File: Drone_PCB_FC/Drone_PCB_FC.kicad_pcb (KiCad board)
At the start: 2 copper layers, 59 parts, among them CN1 SM10B-SRSS-TB, J1 Conn_01x05, J2 USB_C_Receptacle_USB2.0_14P, J3 Conn_01x04, SW1 SW_Push, SW2 SW_Push, U1 AP2112K-3.3, U2 USBLC6-2SC6, U4 STM32F405RGTx, U5 TPS5430DDAR, U6 ICM-42605, U7 W25Q128JVE, Y1 8MHz

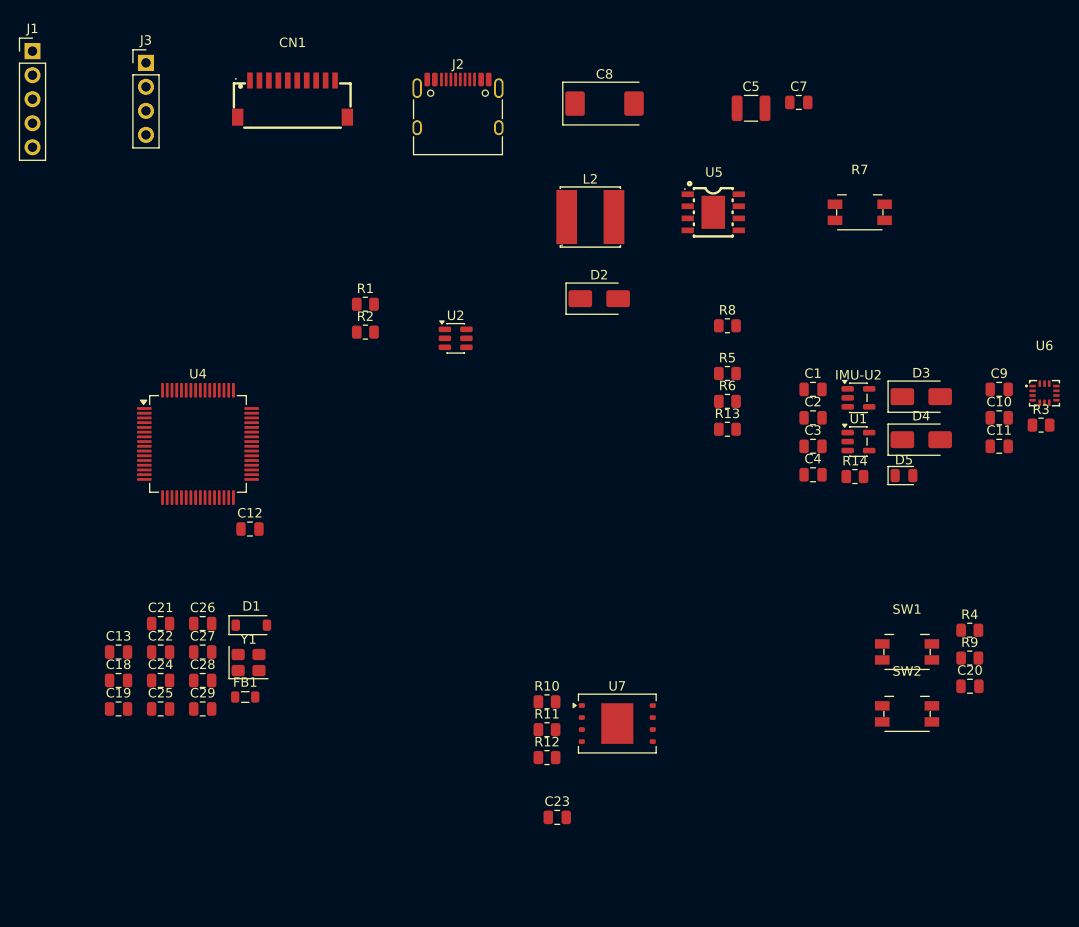
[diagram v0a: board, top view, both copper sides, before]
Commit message: pcb is 'done' but i think i messed up the IMU so ill fix later
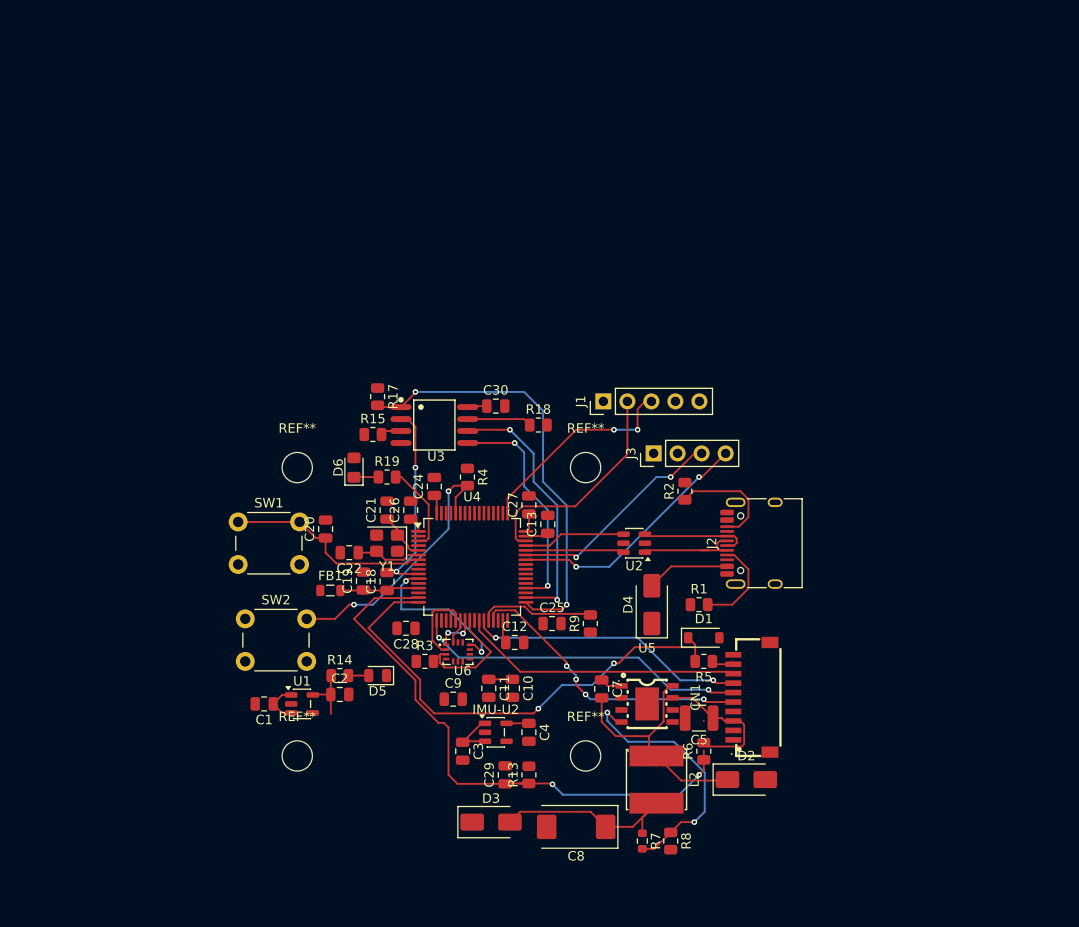
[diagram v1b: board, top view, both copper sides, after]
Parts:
- removed C23: 100nF, Capacitor_SMD:C_0805_2012Metric
- removed R10, R11, R12: 10k, Resistor_SMD:R_0805_2012Metric
- removed U7: W25Q128JVE, Package_SON:WSON-8-1EP_8x6mm_P1.27mm_EP3.4x4.3mm
- added C30: 100nF, Capacitor_SMD:C_0805_2012Metric, F.Cu at (124.5, 78.5)
- added D6: LED, LED_SMD:LED_0805_2012Metric_Pad1.15x1.40mm_HandSolder, F.Cu at (109.5, 85.0)
- added R15: 10k, Resistor_SMD:R_0805_2012Metric, F.Cu at (111.5, 81.5)
- added R17: 10k, Resistor_SMD:R_0805_2012Metric, F.Cu at (112.0, 77.5)
- added R18: 10k, Resistor_SMD:R_0805_2012Metric, F.Cu at (129.0, 80.5)
- added R19: 330, Resistor_SMD:R_0805_2012Metric, F.Cu at (113.0, 86.0)
- added REF**: MountingHole_3.2mm_M3, MountingHole:MountingHole_3.2mm_M3, F.Cu at (134.0, 85.0)
- added REF**: MountingHole_3.2mm_M3, MountingHole:MountingHole_3.2mm_M3, F.Cu at (103.5, 115.5)
- added REF**: MountingHole_3.2mm_M3, MountingHole:MountingHole_3.2mm_M3, F.Cu at (103.5, 85.0)
- added REF**: MountingHole_3.2mm_M3, MountingHole:MountingHole_3.2mm_M3, F.Cu at (134.0, 115.5)
- added U3: W25Q128JVSIQTR, drone_lib:SOIC-8_L5.3-W5.3-P1.27-LS8.0-BL, F.Cu at (118.0, 80.5)
- R7: footprint Button_Switch_SMD:Panasonic_EVQPUJ_EVQPUA -> Resistor_SMD:R_0603_1608Metric
- SW1, SW2: footprint Button_Switch_SMD:Panasonic_EVQPUJ_EVQPUA -> Button_Switch_THT:SW_PUSH_6mm
- moved CN1 79.8 mm to (151.6, 109.3), turned to 90 degrees
- moved C8 76.6 mm to (133.0, 123.0), turned to 180 degrees
- moved SW1 72.1 mm to (97.2, 90.8)
- moved J1 70.8 mm to (135.9, 78.0), turned to 90 degrees
- moved SW2 70.7 mm to (98.0, 101.0)
- moved R7 70.4 mm to (140.0, 124.5), turned to -90 degrees
- moved C20 70.1 mm to (106.5, 91.5), turned to 90 degrees
- moved R3 69.8 mm to (117.0, 105.5)
- moved U6 67.8 mm to (120.5, 104.5)
- moved J3 67.7 mm to (141.2, 83.5), turned to 90 degrees
- moved C1 66.9 mm to (100.0, 110.0), turned to 180 degrees
- moved C9 66.4 mm to (120.0, 109.5)
- moved C7 65.4 mm to (135.7, 108.4), turned to -90 degrees
- moved U1 65.1 mm to (104.0, 110.0)
- moved C5 64.7 mm to (146.0, 111.5), turned to 180 degrees
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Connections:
- C29 pad 1: Net-(U4-PC2) -> Net-(U4-PA1)
- CN1 pad 5: TIM3_CH2-M4 -> TIM2_CH3-M4
- CN1 pad 6: TIM4_CH1-M3 -> TIM2_CH4-M3
- R13 pad 1: Net-(U4-PC2) -> Net-(U4-PA1)
- R6 pad 1: Net-(U4-PC2) -> Net-(U4-PA1)
- U4 pad 10: Net-(U4-PC2) -> SPI2_MISO
- U4 pad 15: unconnected-(U4-PA1-Pad15) -> Net-(U4-PA1)
- U4 pad 16: unconnected-(U4-PA2-Pad16) -> Net-(D1-K)
- U4 pad 17: unconnected-(U4-PA3-Pad17) -> TIM2_CH4-M3
- U4 pad 25: unconnected-(U4-PC5-Pad25) -> Net-(BZ1-+)
- U4 pad 29: unconnected-(U4-PB10-Pad29) -> TIM2_CH3-M4
- U4 pad 3: unconnected-(U4-PC14-Pad3) -> Net-(U4-PC14)
- U4 pad 35: SPI2_MISO -> unconnected-(U4-PB14-Pad35)
- U4 pad 57: TIM3_CH2-M4 -> unconnected-(U4-PB5-Pad57)
- U4 pad 58: TIM4_CH1-M3 -> unconnected-(U4-PB6-Pad58)
- U4 pad 9: Net-(D1-K) -> unconnected-(U4-PC1-Pad9)
- U6 pad 1: MISO -> MOSI
- U6 pad 10: GND -> +3V3
- U6 pad 11: GND -> EXTI3
- U6 pad 12: nCS -> GND
- U6 pad 13: SPI1_SCK -> GND
- U6 pad 14: MOSI -> MISO
- U6 pad 2: GND -> SPI1_SCK
- U6 pad 3: GND -> nCS
- U6 pad 4: EXTI3 -> GND
- U6 pad 5: +3V3 -> GND
- U6 pad 7: GND -> +3V3_IMU
- U6 pad 8: +3V3_IMU -> GND
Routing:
- net Net-(U4-PA1): track 0.00 -> 60.8 mm, vias 0 -> 2
- net Net-(D1-K): track 0.00 -> 51.6 mm, vias 0 -> 2
- net /CS: track 0.00 -> 45.5 mm, vias 0 -> 2
- net TIM2_CH4-M3: track 0.00 -> 35.5 mm, vias 0 -> 2
- net TIM2_CH3-M4: track 0.00 -> 31.2 mm, vias 0 -> 4
- net TIM3_CH4-M2: track 0.00 -> 30.3 mm, vias 0 -> 2
- net TIM3_CH3-M1: track 0.00 -> 29.8 mm
- net BOOT0: track 0.00 -> 28.6 mm, vias 0 -> 2
- net SPI2_SCK: track 0.00 -> 28.0 mm, vias 0 -> 2
- net Net-(U5-VSENSE): track 0.00 -> 27.7 mm, vias 0 -> 2
- net UARTx_TX: track 0.00 -> 26.4 mm, vias 0 -> 2
- net Net-(D2-K): track 0.00 -> 25.7 mm
- net SPI2_MOSI: track 0.00 -> 23.9 mm, vias 0 -> 2
- net SWDIO: track 0.00 -> 23.9 mm
- net UARTx_RX: track 0.00 -> 23.3 mm, vias 0 -> 2
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- added copper zone on In1.Cu, net GND
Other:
- copper layers 2 -> 4

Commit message: 3rd try on the PCB, still need to triple check before I order, and I NEED to check stock because i might need a redesign
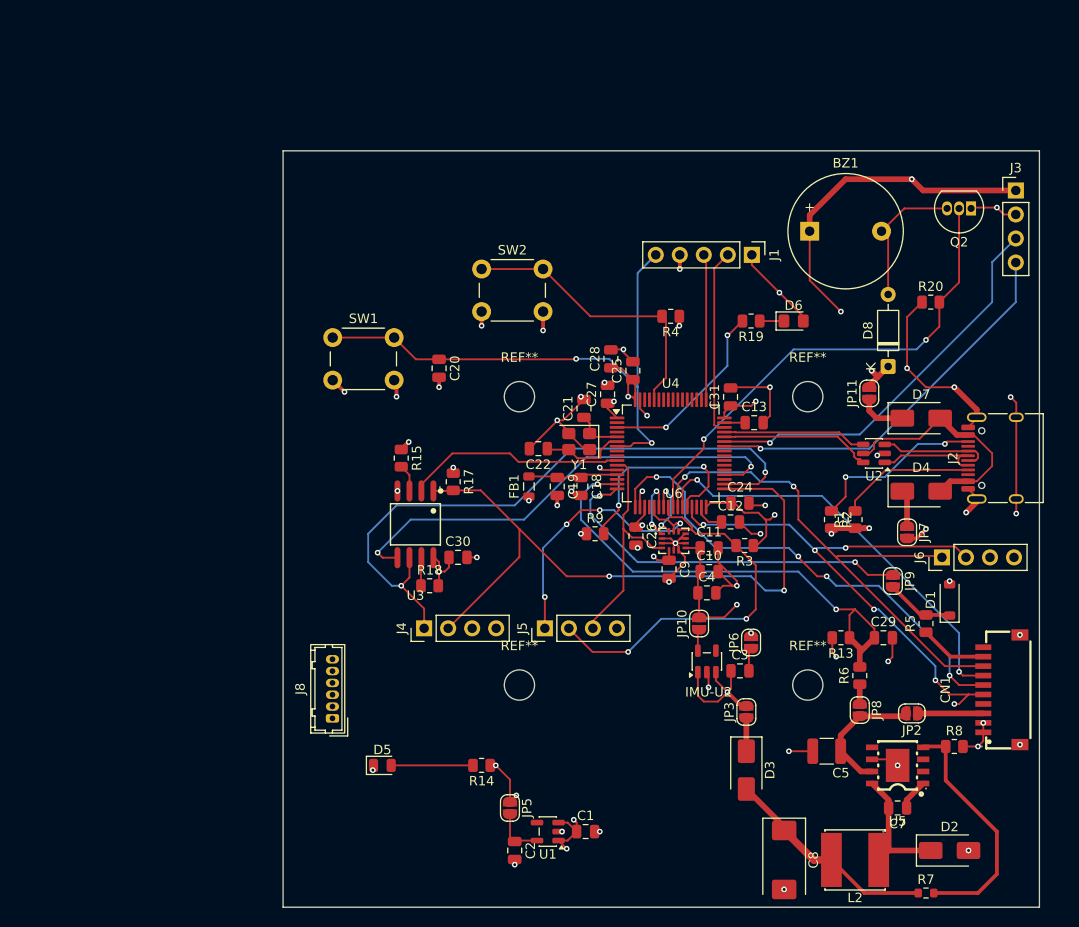
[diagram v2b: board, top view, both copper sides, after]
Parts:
- removed the REF** at (134.0, 85.0)
- removed the REF** at (103.5, 115.5)
- removed the REF** at (103.5, 85.0)
- removed the REF** at (134.0, 115.5)
- added BZ1: Buzzer, Buzzer_Beeper:Buzzer_12x9.5RM7.6, F.Cu at (157.7, 60.0)
- added C31: 100nF, Capacitor_SMD:C_0805_2012Metric, F.Cu at (149.3, 77.5)
- added D7: D_Schottky, Diode_SMD:D_SMA, F.Cu at (169.5, 79.8)
- added D8: 1N914, Diode_THT:D_DO-35_SOD27_P7.62mm_Horizontal, F.Cu at (166.0, 74.3)
- added J4: Conn_01x04, Connector_PinHeader_2.54mm:PinHeader_1x04_P2.54mm_Vertical, F.Cu at (116.9, 102.0)
- added J5: Conn_01x04, Connector_PinHeader_2.54mm:PinHeader_1x04_P2.54mm_Vertical, F.Cu at (129.7, 102.0)
- added J6: Conn_01x04, Connector_PinHeader_2.54mm:PinHeader_1x04_P2.54mm_Vertical, F.Cu at (171.7, 94.5)
- added J8: Conn_01x06, Connector_Hirose:Hirose_DF13-06P-1.25DSA_1x06_P1.25mm_Vertical, F.Cu at (107.2, 111.5)
- added JP10: SolderJumper_2_Open, Jumper:SolderJumper-2_P1.3mm_Open_RoundedPad1.0x1.5mm, F.Cu at (146.0, 101.5)
- added JP11: SolderJumper_2_Open, Jumper:SolderJumper-2_P1.3mm_Open_RoundedPad1.0x1.5mm, F.Cu at (164.0, 77.2)
- added JP2: SolderJumper_2_Open, Jumper:SolderJumper-2_P1.3mm_Open_RoundedPad1.0x1.5mm, F.Cu at (168.5, 111.0)
- added JP3: SolderJumper_2_Open, Jumper:SolderJumper-2_P1.3mm_Open_RoundedPad1.0x1.5mm, F.Cu at (151.0, 110.8)
- added JP5: SolderJumper_2_Open, Jumper:SolderJumper-2_P1.3mm_Open_RoundedPad1.0x1.5mm, F.Cu at (126.0, 121.0)
- added JP6: SolderJumper_2_Open, Jumper:SolderJumper-2_P1.3mm_Open_RoundedPad1.0x1.5mm, F.Cu at (151.5, 103.5)
- added JP7: SolderJumper_2_Open, Jumper:SolderJumper-2_P1.3mm_Open_RoundedPad1.0x1.5mm, F.Cu at (168.0, 91.8)
- added JP8: SolderJumper_2_Open, Jumper:SolderJumper-2_P1.3mm_Open_RoundedPad1.0x1.5mm, F.Cu at (163.0, 110.7)
- added JP9: SolderJumper_2_Open, Jumper:SolderJumper-2_P1.3mm_Open_RoundedPad1.0x1.5mm, F.Cu at (166.5, 97.0)
- added Q2: 2N7000, Package_TO_SOT_THT:TO-92_Inline, F.Cu at (174.8, 57.6)
- added R20: 10k, Resistor_SMD:R_0805_2012Metric, F.Cu at (170.5, 67.5)
- added REF**: MountingHole_3.2mm_M3, MountingHole:MountingHole_3.2mm_M3, F.Cu at (127.0, 108.0)
- added REF**: MountingHole_3.2mm_M3, MountingHole:MountingHole_3.2mm_M3, F.Cu at (157.5, 77.5)
- added REF**: MountingHole_3.2mm_M3, MountingHole:MountingHole_3.2mm_M3, F.Cu at (127.0, 77.5)
- added REF**: MountingHole_3.2mm_M3, MountingHole:MountingHole_3.2mm_M3, F.Cu at (157.5, 108.0)
- moved D6 49.0 mm to (156.0, 69.5), turned to 0 degrees
- moved J3 47.3 mm to (179.5, 55.7), turned to 0 degrees
- moved SW2 44.7 mm to (123.0, 64.0)
- moved C29 42.5 mm to (165.5, 103.0), turned to 0 degrees
- moved R19 41.9 mm to (151.5, 69.5), turned to 180 degrees
- moved C1 36.6 mm to (134.0, 123.5), turned to 0 degrees
- moved R13 36.0 mm to (161.0, 103.0), turned to 180 degrees
- moved R3 36.0 mm to (150.8, 93.2), turned to 180 degrees
- moved C28 35.8 mm to (136.7, 73.5), turned to 90 degrees
- moved C7 33.7 mm to (167.0, 121.0), turned to 180 degrees
- moved C24 32.4 mm to (150.3, 88.8), turned to 0 degrees
- moved R8 31.6 mm to (173.0, 114.5), turned to 0 degrees
- moved D4 30.9 mm to (169.5, 87.5), turned to 0 degrees
- moved C3 30.5 mm to (150.3, 106.5), turned to 0 degrees
- moved R7 30.5 mm to (170.0, 130.0), turned to 0 degrees
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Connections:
- net Net-(J2-D+-PadA6) renamed in_USB_D+
- net Net-(J2-D--PadA7) renamed in_USB_D-
- net /CS renamed Flash_/CS
- C2 pad 1: +3V3 -> Net-(JP5-B)
- C3 pad 2: GND -> Net-(JP6-A)
- C5 pad 1: +BATT -> +BATT_after
- D3 pad 1: +5V -> Net-(D3-K)
- D4 pad 1: +5V -> Net-(D4-K)
- IMU-U2 pad 5: +3V3_IMU -> Net-(IMU-U2-OUT)
- R3 pad 2: nCS -> IMU_nCS
- R6 pad 1: Net-(U4-PA1) -> Net-(JP8-A)
- R6 pad 2: +BATT -> Net-(U4-PA1)
- U1 pad 5: +3V3 -> Net-(JP5-B)
- U4 pad 16: Net-(D1-K) -> Net-(JP9-A)
- U4 pad 24: nCS -> IMU_nCS
- U4 pad 39: unconnected-(U4-PC8-Pad39) -> PC8
- U4 pad 40: unconnected-(U4-PC9-Pad40) -> PC9
- U4 pad 41: unconnected-(U4-PA8-Pad41) -> PA8
- U4 pad 51: unconnected-(U4-PC10-Pad51) -> PC10
- U4 pad 52: unconnected-(U4-PC11-Pad52) -> PC11
- U4 pad 55: unconnected-(U4-PB3-Pad55) -> PB3
- U5 pad 7: +BATT -> +BATT_after
- U6 pad 1: MOSI -> MISO
- U6 pad 10: +3V3 -> GND
- U6 pad 11: EXTI3 -> GND
- U6 pad 12: GND -> IMU_nCS
- U6 pad 13: GND -> SPI1_SCK
- U6 pad 14: MISO -> MOSI
- U6 pad 2: SPI1_SCK -> GND
- U6 pad 3: nCS -> GND
- U6 pad 4: GND -> EXTI3
- U6 pad 5: GND -> +3V3
- U6 pad 7: +3V3_IMU -> GND
- U6 pad 8: GND -> +3V3_IMU
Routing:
- net GND: track 0.28 -> 136.7 mm, vias 0 -> 50
- net +5V: track 10.2 -> 62.9 mm, vias 0 -> 7
- net Net-(Q2-G): track 0.00 -> 51.7 mm, vias 0 -> 2
- net +3V3: track 13.8 -> 61.1 mm, vias 0 -> 15
- net Net-(D1-K): track 51.6 -> 7.24 mm, vias 2 -> 0
- net IMU_nCS: track 0.00 -> 41.3 mm, vias 0 -> 2
- net SPI2_SCK: track 28.0 -> 68.8 mm
- net Net-(JP9-A): track 0.00 -> 39.5 mm, vias 0 -> 2
- net NRST: track 22.0 -> 60.4 mm, vias 0 -> 2
- net TIM2_CH3-M4: track 31.2 -> 59.1 mm, vias 4 -> 6
- net TIM3_CH3-M1: track 29.8 -> 56.9 mm, vias 0 -> 2
- net Flash_/CS: track 45.5 -> 71.5 mm
- net SPI2_MOSI: track 23.9 -> 49.8 mm
- net SPI1_SCK: track 8.27 -> 31.5 mm, vias 0 -> 4
- net UARTx_RX: track 23.3 -> 43.1 mm, vias 2 -> 1
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- added copper zone on In2.Cu, net +3V3
- added copper zone on In2.Cu, net +3V3_IMU
- added copper zone on In2.Cu, net +5V
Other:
- board outline added: 80 x 80 mm

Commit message: Ordered the PCB now i have to wait and see if i waisted 130 dollars
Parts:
- removed C10: 2.2uF, Capacitor_SMD:C_0805_2012Metric
- removed C11: .1uF, Capacitor_SMD:C_0805_2012Metric
- removed C9: 10nF, Capacitor_SMD:C_0805_2012Metric
- removed D2: SS34, Diode_SMD:D_SMA
- removed J8: Conn_01x06, Connector_Hirose:Hirose_DF13-06P-1.25DSA_1x06_P1.25mm_Vertical
- removed U6: ICM-42605, drone_lib:LGA-14_L3.0-W2.5-P0.50-TL
- added C14: 100nF, Capacitor_SMD:C_0805_2012Metric, F.Cu at (145.0, 92.5)
- added C15: 100nF, Capacitor_SMD:C_0805_2012Metric, F.Cu at (142.0, 95.0)
- added D9: D_Schottky, Diode_SMD:D_SMA, F.Cu at (168.5, 125.8)
- added J7: Conn_01x06, Connector_PinSocket_2.54mm:PinSocket_1x06_P2.54mm_Vertical, F.Cu at (106.3, 99.8)
- added U7: BMI270, drone_lib:LGA-14_L3.0-W2.5-P0.50-BR, F.Cu at (142.5, 92.5)
- 3.2mm M3: renamed from REF** (x4)
- CurrentM1: renamed from JP9; value SolderJumper_2_Open -> Current M
- R7: footprint Resistor_SMD:R_0603_1608Metric -> Resistor_SMD:R_0805_2012Metric_Pad1.20x1.40mm_HandSolder
- U3: value W25Q128JVSIQTR -> GD25Q16ETIGR
- moved R9 19.1 mm to (152.7, 84.9), turned to 180 degrees
- moved R2 13.5 mm to (170.2, 81.6), turned to 180 degrees
- moved R7 12.7 mm to (172.0, 117.5), turned to 90 degrees
- moved JP8 9.39 mm to (159.0, 102.2), turned to 90 degrees
- moved R1 9.02 mm to (169.9, 85.4), turned to 0 degrees
- moved USB5V1 5.28 mm to (164.0, 88.5), turned to 180 degrees
- moved C22 3.85 mm to (132.4, 84.9)
- moved C29 3.16 mm to (164.5, 106.0)
- moved JP10 2.55 mm to (145.5, 99.0)
- moved C4 2.40 mm to (146.0, 96.0)
- moved R3 2.34 mm to (148.5, 93.0)
- moved FB1 2.24 mm to (130.0, 88.0)
- moved D1 2.12 mm to (174.0, 100.5), turned to 0 degrees
- moved R6 2.00 mm to (163.0, 109.0)
- moved R13 1.58 mm to (161.5, 104.5), turned to 90 degrees
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- renumbered JP7 to USB5V1, JP11 to USB5V2
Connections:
- C29 pad 1: Net-(U4-PA1) -> Net-(JP8-A)
- J6 pad 2: TIM2_CH3-M4 -> TIM3_CH4-M2
- J6 pad 3: GND -> TIM2_CH4-M3
- J6 pad 4: GND -> TIM2_CH3-M4
- JP2 pad 1: +BATT -> +BATT_after
- JP2 pad 2: +BATT_after -> +BATT
- JP8 pad 2: +BATT_after -> Net-(JP8-B)
- R13 pad 1: Net-(U4-PA1) -> Net-(JP8-A)
- R6 pad 1: Net-(JP8-A) -> +BATT_after
- R6 pad 2: Net-(U4-PA1) -> Net-(JP8-A)
- U2 pad 5: +5V_USB -> +5V
- U4 pad 15: Net-(U4-PA1) -> Net-(JP8-B)
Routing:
- net PC9: track 0.00 -> 93.4 mm, vias 0 -> 2
- net PB3: track 0.00 -> 77.7 mm, vias 0 -> 2
- net PC11: track 0.00 -> 70.1 mm, vias 0 -> 2
- net PC10: track 0.00 -> 69.4 mm, vias 0 -> 2
- net PA8: track 0.00 -> 65.9 mm, vias 0 -> 2
- net PC8: track 0.00 -> 63.3 mm, vias 0 -> 2
- net Net-(U4-PA1): track 52.6 -> 0.00 mm, vias 2 -> 0
- net Net-(JP8-B): track 0.00 -> 37.4 mm, vias 0 -> 2
- net GND: track 136.7 -> 113.5 mm, vias 50 -> 56
- net Net-(U5-VSENSE): track 25.7 -> 4.46 mm
- net Net-(J2-CC2): track 18.7 -> 3.82 mm, vias 2 -> 0
- net SPI2_SCK: track 68.8 -> 55.0 mm
- net +5V_Buck: track 23.0 -> 36.6 mm
- net TIM2_CH4-M3: track 51.1 -> 63.5 mm, vias 4 -> 2
- net +3V3: track 61.1 -> 48.8 mm, vias 15 -> 16
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- added copper zone on F.Cu, net GND
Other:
- board text added: "+"
- board text added: "+BATT"
- board text added: "-"
- board text added: ".01uF"
- board text added: "100K"
- board text added: "100nF"
- board text added: "10K"
- board text added: "10k"
- board text added: "10nF"
- board text added: "10uF"
- board text added: "15uH"
- board text added: "1k"
- board text added: "1uF"
- board text added: "2.2uF"
- board text added: "220uF"
- board text added: "22pF"
- board text added: "2N7000 MOSFET"
- board text added: "3.24k"
- board text added: "330"
- board text added: "3V3"
- board text added: "3V3 IMU"
- board text added: "4.7uF"
- board text added: "470"
- board text added: "5V"
- board text added: "600@ 100MHz"
- board text added: "ETHAN SUTTOR 7/19/26"
- board text added: "EXIT3"
- board text added: "Flash/cs"
- board text added: "GND"
- board text added: "IMU_nCS"
- board text added: "LED"
- board text added: "M1"
- board text added: "M3"
- board text added: "M4"
- board text added: "PA8"
- board text added: "PB3"
- board text added: "PC10"
- board text added: "PC11"
- board text added: "PC8"
- board text added: "PC9"
- board text added: "RESET"
- board text added: "RX"
- board text added: "SPI1_SCK"
- board text added: "SPI2_SCK"
- board text added: "SWDCLK"
- board text added: "SWDIO"
- board text added: "Schottky"
- board text added: "TX"
- board text added: "VBAT"
